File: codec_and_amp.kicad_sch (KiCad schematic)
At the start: 32 parts, among them J1 Conn_01x08, J2 Conn_01x06, U1 TLV320AIC3206IRSBR, U4 FSA2275UMX, U6 MIC5504-1.8YM5, U7 TPD4E02B04DQAR, U8 TPD4E02B04DQAR

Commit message: Update to Kicad 6.0.0
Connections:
- net ~CODEC_RESET renamed ~{CODEC_RESET}
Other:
- sheet spkr_amp_left ports: added ~{SHUTDOWN}; removed ~SHUTDOWN
- sheet spkr_amp_right ports: added ~{SHUTDOWN}; removed ~SHUTDOWN

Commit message: Remove tlv320aic3206 and bq25895 and supporting circuitry from schematic; wire up audio/battery connections to Radxa CM3 third connector instead.
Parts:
- removed C1, C11, C24: 100nF, Capacitor_SMD:C_0402_1005Metric, symbol Device:C
- removed C10, C13, C14, C23, C4, C54: 10uF, Capacitor_SMD:C_0402_1005Metric, symbol Device:C
- removed C12, C9: 0.1u, Capacitor_SMD:C_0402_1005Metric, symbol Device:C
- removed C15, C22, C8: 0.1uF, Capacitor_SMD:C_0402_1005Metric, symbol Device:C
- removed C2: 1uF, Capacitor_SMD:C_0402_1005Metric, symbol Device:C
- removed C3, C5: 2.2uF, Capacitor_SMD:C_0402_1005Metric, symbol Device:C
- removed R1: 2.7k, Resistor_SMD:R_0402_1005Metric, symbol Device:R
- removed R10, R7, R8, R9: 27, Resistor_SMD:R_0402_1005Metric, symbol Device:R
- removed R2, R3, R6: 1k, Resistor_SMD:R_0402_1005Metric, symbol Device:R
- removed U1: TLV320AIC3206IRSBR, footprints:TLV320AIC3206IRSBR, symbol TLV320AIC3206IRSBR:TLV320AIC3206IRSBR
- removed U4: FSA2275UMX, footprints:FSA2275, symbol FSA2275UMX:FSA2275UMX
- removed U6: MIC5504-1.8YM5, Package_TO_SOT_SMD:SOT-23-5, symbol Regulator_Linear:MIC5504-1.8YM5
- added C? (x3): 0.1uF, Capacitor_SMD:C_0402_1005Metric, symbol Device:C
- added Module?: ComputeModule4-CM4, CM4IO:Raspberry-Pi-4-Compute-Module, symbol CM4IO:ComputeModule4-CM4
- added R? (x3): 1k, Resistor_SMD:R_0402_1005Metric, symbol Device:R
- added R? (x4): 0, symbol Device:R
- added U? (x3): FSA2275UMX, footprints:FSA2275, symbol FSA2275UMX:FSA2275UMX
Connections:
- net GND: now also C?.2, C?.2, C?.2, R?.1, R?.2, R?.2, R?.2, U?.3 (GND), U?.3 (GND), U?.3 (GND), U?.8 (GND), U?.8 (GND), U?.8 (GND)
- net INTMIC_N: now also U?.10 (R1)
- net INTMIC_P: now also U?.12 (L1)
- net LOL: now also U?.12 (L1)
- net LOR: now also U?.10 (R1)
- net RING1: now also U?.9 (R2)
- net RING2: now also R?.2, U?.11 (L2), U?.9 (R2), U?.9 (R2)
- net SLEEVE: now also U?.11 (L2)
- net TIP: now also U?.11 (L2)
- net VSYS: now also U?.1 (VDD), U?.1 (VDD), U?.1 (VDD)
- net spkr_amp_left/SPKR+ renamed SPK1P
- net SPK1P: now also Module?.260 (SPKP_OUT), R?.1
- net spkr_amp_left/SPKR- renamed SPK1N
- net SPK1N: now also R?.1, R?.2
- net spkr_amp_right/SPKR+ renamed SPK2P
- net SPK2P: now also R?.2, R?.2
- net spkr_amp_right/SPKR- renamed SPK2N
- net SPK2N: now also Module?.258 (SPKN_OUT), R?.1
- new net: R?.1, U?.7 (MUTE) (x3)
- new net: C?.1, U?.2 (C_EXT) (x3)
- new net: Module?.252 (HP_SNS), U?.4 (LSPKR), U?.5 (RSPKR)
- new net: Module?.250 (HPL_OUT), U?.4 (LSPKR)
- new net: Module?.254 (HPR_OUT), U?.5 (RSPKR)
- new net: Module?.264 (MIC1_IN), U?.4 (LSPKR)
- new net: Module?.266 (MIC2_IN), U?.5 (RSPKR)
- new net HP_LINEOUT_SELECT: U?.6 (SEL), U?.6 (SEL)
- new net LO_REF: U?.10 (R1), U?.12 (L1)
- new net MIC_SELECT: U?.6 (SEL)
- no-connect marks 3 -> 0
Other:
- removed sheet spkr_amp_left
- removed sheet spkr_amp_right
- moved on the sheet: J1, J2, U7, U8

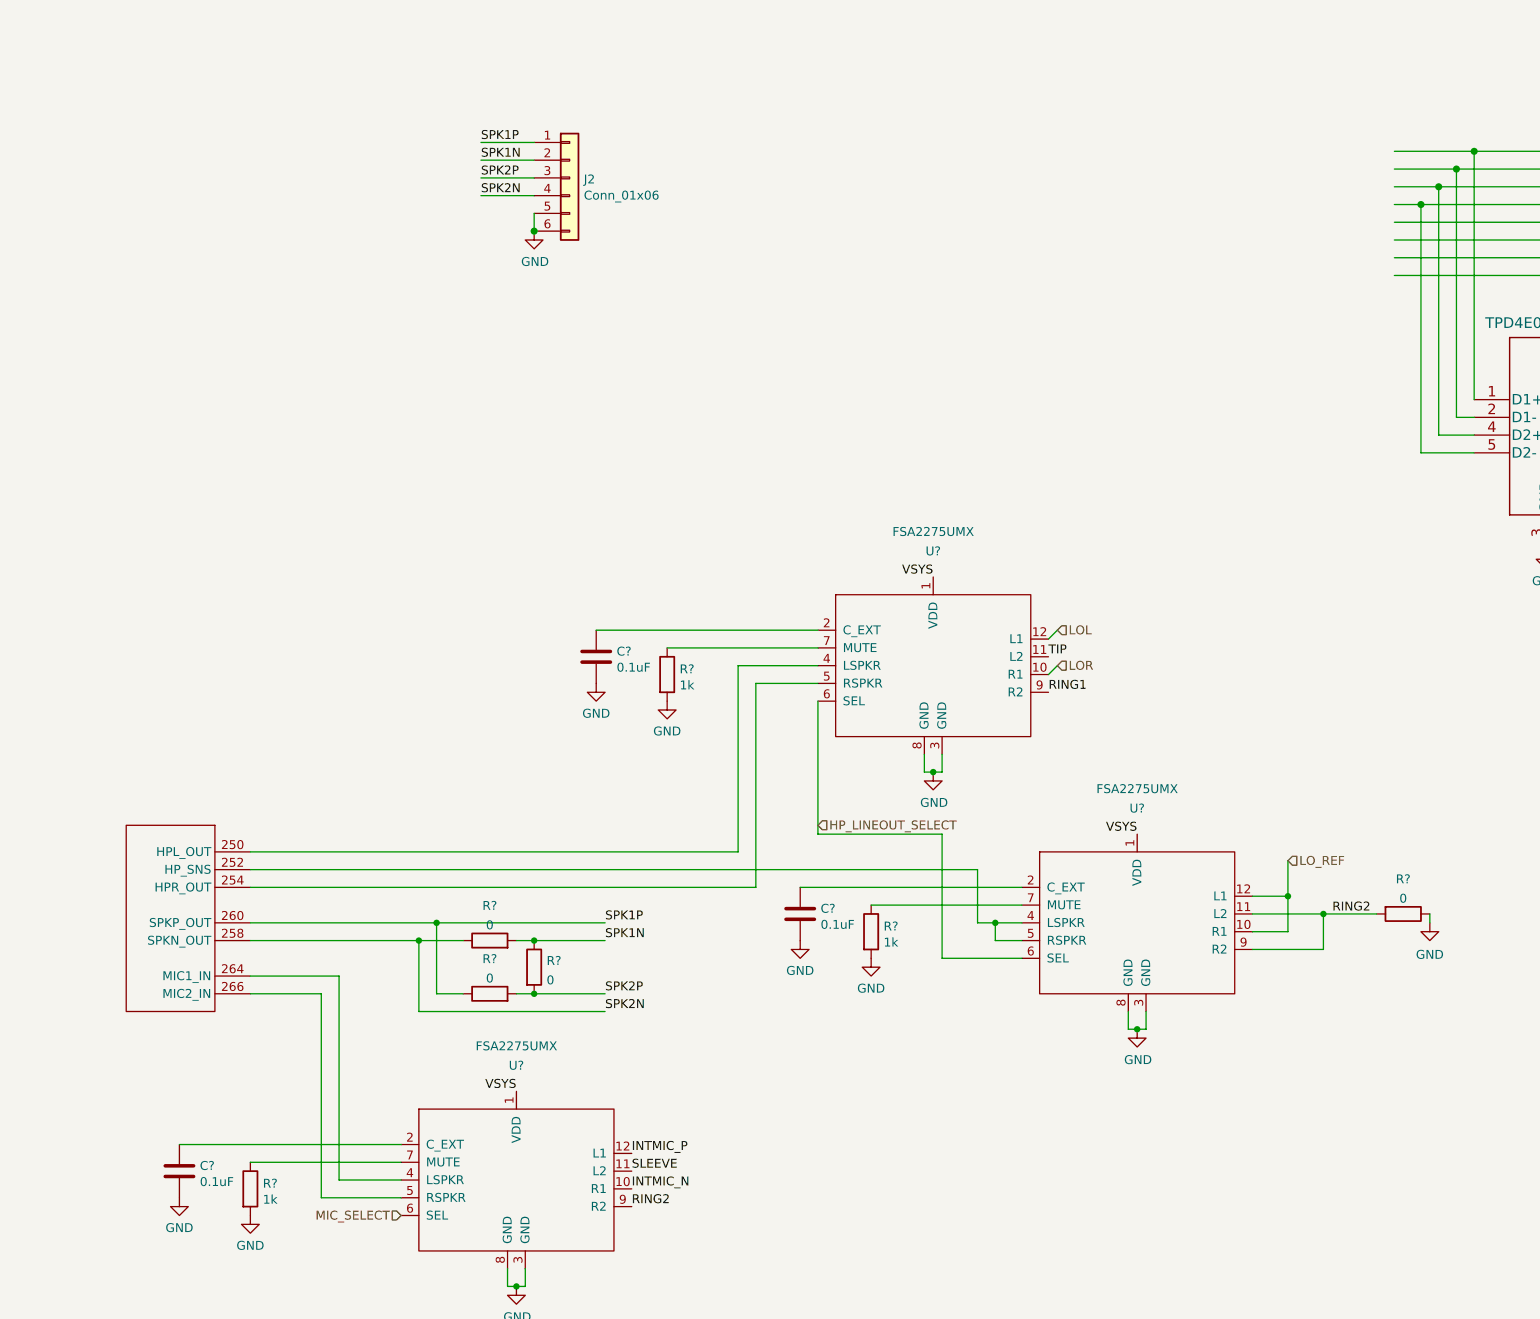
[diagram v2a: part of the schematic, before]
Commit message: Lots of changes to convert to Radxa CM3. Also reroute all the touchscreen connections with smaller tolerances, which avoids having to route anything on inner layers.
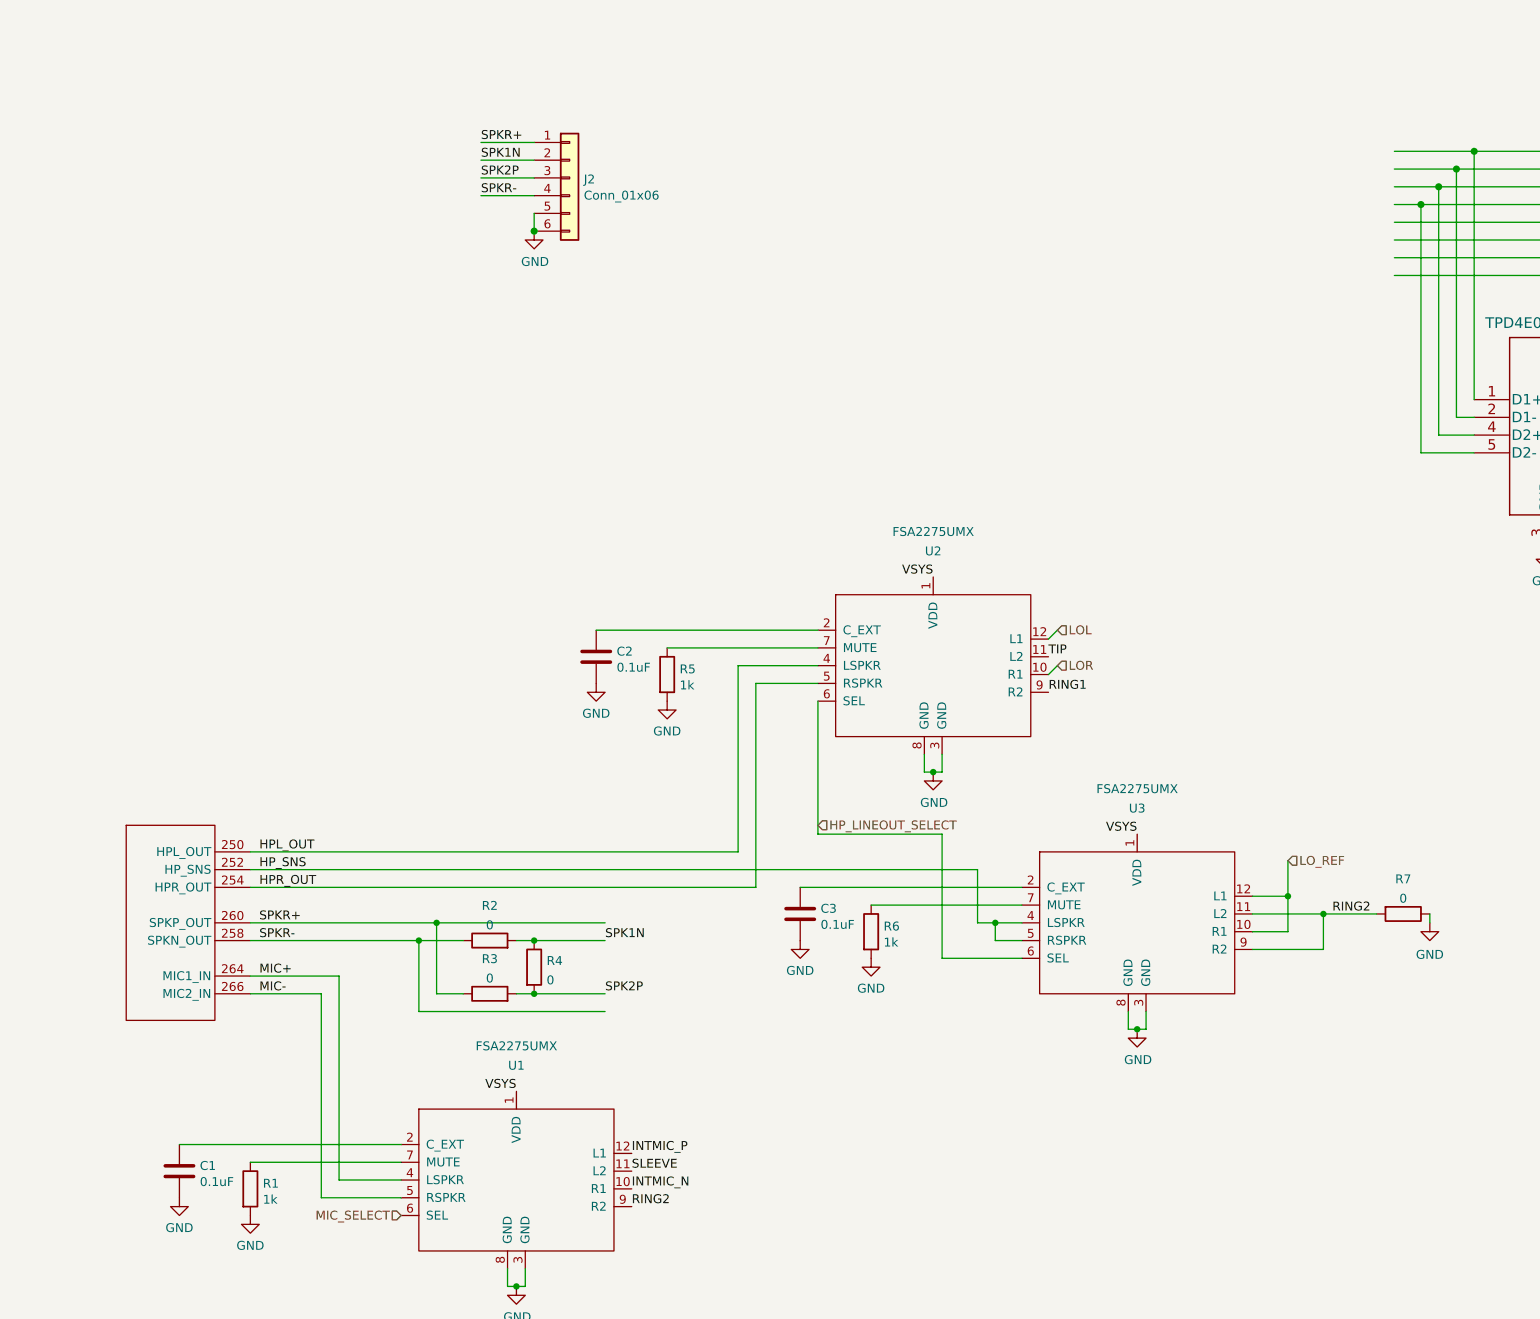
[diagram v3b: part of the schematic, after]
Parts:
- Module1: renamed from Module?; footprint CM4IO:Raspberry-Pi-4-Compute-Module -> footprints:Raspberry-Pi-4-Compute-Module
- R2, R3, R4, R7: renamed from R?; footprint (none) -> Resistor_SMD:R_0402_1005Metric
- gave numbers to parts that had none: 9
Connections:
- net HP_SNS: now reaches Module1.252 (HP_SNS), U3.4 (LSPKR), U3.5 (RSPKR)
- net HPL_OUT: now reaches Module1.250 (HPL_OUT), U2.4 (LSPKR)
- net HPR_OUT: now reaches Module1.254 (HPR_OUT), U2.5 (RSPKR)
- net MIC+: now reaches Module1.264 (MIC1_IN), U1.4 (LSPKR)
- net MIC-: now reaches Module1.266 (MIC2_IN), U1.5 (RSPKR)
- net SPK1P renamed SPKR+
- net SPK2N renamed SPKR-

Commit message: Lots more work on the cm3 version of this board.
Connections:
- net DETECT?: now also Module1.236 (HP_DET_L)
- net HPL_OUT: now also U2.5 (RSPKR); no longer U2.4 (LSPKR)
- net HPR_OUT: now also U2.4 (LSPKR); no longer U2.5 (RSPKR)
- net LOL: now also U2.10 (R1); no longer U2.12 (L1)
- net LOR: now also U2.12 (L1); no longer U2.10 (R1)
- net RING1: now also U2.11 (L2); no longer U2.9 (R2)
- net TIP: now also U2.9 (R2); no longer U2.11 (L2)

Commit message: Final touches on Radxa CM3 version of the board
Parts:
- Module1: value ComputeModule4-CM4 -> Radxa CM3; symbol CM4IO:ComputeModule4-CM4 -> CM4IO:Radxa CM3
- renumbered R7 to JP7
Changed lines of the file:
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@@
   (symbol (lib_id "Device:R") (at 278.13 172.72 270) (unit 1)
     (in_bom yes) (on_board yes) (fields_autoplaced)
-    (property "Reference" "R7" (id 0) (at 278.13 167.7375 90))
+    (property "Reference" "JP7" (id 0) (at 278.13 167.7375 90))
     (property "Value" "0" (id 1) (at 278.13 170.5126 90))
     (property "Footprint" "Resistor_SMD:R_0402_1005Metric" (id 2) (at 278.13 170.942 90)
@@
     (pin "2")
   )
-  (symbol (lib_id "CM4IO:ComputeModule4-CM4") (at 101.6 172.72 0) (unit 7)
+  (symbol (lib_id "CM4IO:Radxa CM3") (at 101.6 172.72 0) (unit 7)
     (in_bom yes) (on_board yes) (fields_autoplaced)
     (property "Reference" "Module1" (id 0) (at 101.6 181.61 0)
       (effects (font (size 1.27 1.27)) hide)
     )
-    (property "Value" "ComputeModule4-CM4" (id 1) (at 102.87 165.1 0)
+    (property "Value" "Radxa CM3" (id 1) (at 102.87 165.1 0)
       (effects (font (size 1.27 1.27)) hide)
     )
@@
       (effects (font (size 1.27 1.27)) hide)
     )
-    (property "Field4" "Hirose" (id 4) (at 101.6 172.72 0)
-      (effects (font (size 1.27 1.27)) hide)
-    )
-    (property "Field5" "2x DF40C-100DS-0.4V" (id 5) (at 101.6 175.26 0)
-      (effects (font (size 1.27 1.27)) hide)
-    )
+    (property "Field4" "Hirose" (id 4) (at 92.71 172.72 0)
+      (effects (font (size 1.27 1.27)) hide)
+    )
+    (property "Field5" "2x DF40C-100DS-0.4V" (id 5) (at 92.71 175.26 0)
+      (effects (font (size 1.27 1.27)) hide)
+    )
